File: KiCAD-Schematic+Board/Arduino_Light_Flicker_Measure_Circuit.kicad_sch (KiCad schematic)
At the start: 42 parts, among them J1 Ds, J2 Ds, J3 FTDI, J4 FTDI-Conn, J5 PWR(5V), J6 USB Power (5V), Q1 BC547, Q2 BC547, U1 ATmega328P-PU, U2 AD5242, U3 AD823A, U4 Display

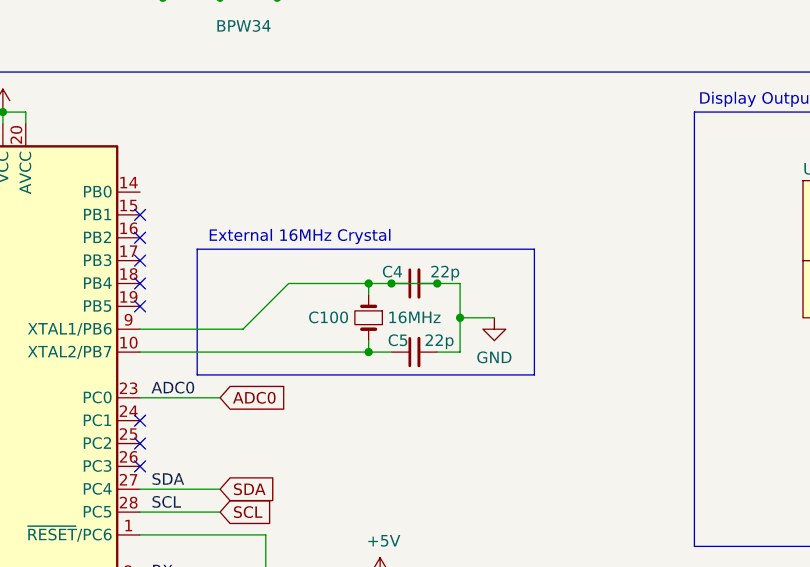
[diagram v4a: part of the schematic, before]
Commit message: Small update to add Pro Mini footprint to get rid of original footprint stuff hopefully.
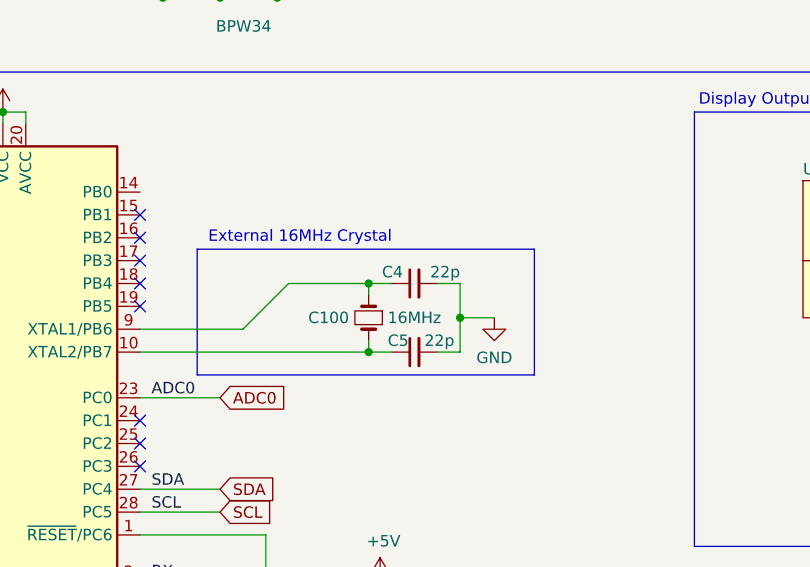
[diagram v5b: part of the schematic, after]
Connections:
- net GND: no longer C100.1, C4.1, U1.9 (XTAL1/PB6)
- new net: C100.1, C4.1, U1.9 (XTAL1/PB6)
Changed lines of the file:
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@@
   (junction (at 67.31 96.52) (diameter 0) (color 0 0 0 0)
   )
-  (junction (at 97.79 128.27) (diameter 0) (color 0 0 0 0)
-  )
   (junction (at 124.46 78.74) (diameter 0) (color 0 0 0 0)
   )
@@
   )
   (junction (at 49.53 109.22) (diameter 0) (color 0 0 0 0)
-  )
-  (junction (at 92.71 128.27) (diameter 0) (color 0 0 0 0)
   )
   (junction (at 80.01 82.55) (diameter 0) (color 0 0 0 0)
@@
     (stroke (width 0) (type default))
   )
+  (wire (pts (xy 97.79 128.27) (xy 100.33 128.27))
+    (stroke (width 0) (type default))
+  )
   (wire (pts (xy 82.55 46.99) (xy 82.55 63.5))
     (stroke (width 0) (type default))
@@
     (stroke (width 0) (type default))
   )
-  (wire (pts (xy 97.79 128.27) (xy 100.33 128.27))
-    (stroke (width 0) (type default))
-  )
   (wire (pts (xy 50.8 34.29) (xy 50.8 27.94))
     (stroke (width 0) (type default))
@@
     (stroke (width 0) (type default))
   )
-  (wire (pts (xy 92.71 128.27) (xy 90.17 128.27))
-    (stroke (width 0) (type default))
-  )
   (wire (pts (xy 158.75 97.79) (xy 158.75 91.44))
     (stroke (width 0) (type default))
@@
     (stroke (width 0) (type default))
   )
-  (wire (pts (xy 92.71 128.27) (xy 97.79 128.27))
-    (stroke (width 0) (type default))
-  )
   (wire (pts (xy 158.75 83.82) (xy 158.75 78.74))
     (stroke (width 0) (type default))
@@
     (stroke (width 0) (type default))
   )
+  (wire (pts (xy 90.17 128.27) (xy 92.71 128.27))
+    (stroke (width 0) (type default))
+  )

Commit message: Update to do basic messed-up layout.  Imperfect but hopefully functional.
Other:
- note added: "Digipot (0 or 1M) to ON/OFF 3 BPW34"
- note removed: "Digital Poti (0 or 1M) to ON/OFF 3 BPW34"
- moved on the sheet: J1
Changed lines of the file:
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@@
     (stroke (width 0) (type default))
   )
-  (wire (pts (xy 77.47 62.23) (xy 77.47 66.04))
+  (wire (pts (xy 77.47 62.23) (xy 77.47 64.77))
     (stroke (width 0) (type default))
   )
@@
     (stroke (width 0) (type default))
   )
-  (wire (pts (xy 82.55 66.04) (xy 82.55 63.5))
+  (wire (pts (xy 82.55 64.77) (xy 82.55 63.5))
     (stroke (width 0) (type default))
   )
@@
     (stroke (width 0) (type default))
   )
-  (wire (pts (xy 80.01 49.53) (xy 80.01 66.04))
+  (wire (pts (xy 80.01 49.53) (xy 80.01 64.77))
     (stroke (width 0) (type default))
   )
@@
     (effects (font (size 1.27 1.27)))
   )
-  (text "Digital Poti (0 or 1M)\nto ON/OFF 3 BPW34\n" (exclude_from_sim no)
+  (text "Digipot (0 or 1M)\nto ON/OFF 3 BPW34\n" (exclude_from_sim no)
  (at 88.9 43.815 0)
     (effects (font (size 1.27 1.27)))
@@
     )
   )
-  (symbol (lib_id "Connector_Generic:Conn_01x03") (at 80.01 71.12 90) (mirror x) (unit 1)
-    (exclude_from_sim no) (in_bom yes) (on_board yes) (dnp no)
-    (property "Reference" "J1" (at 84.7852 67.8942 90)
+  (symbol (lib_id "Connector_Generic:Conn_01x03") (at 80.01 69.85 90) (mirror x) (unit 1)
+    (exclude_from_sim no) (in_bom yes) (on_board yes) (dnp no)
+    (property "Reference" "J1" (at 84.7852 66.6242 90)
       (effects (font (size 1.27 1.27)) (justify right))
     )
-    (property "Value" "Ds" (at 84.7852 70.2056 90)
+    (property "Value" "Ds" (at 84.7852 68.9356 90)
       (effects (font (size 1.27 1.27)) (justify right))
     )
-    (property "Footprint" "Connector_PinHeader_2.54mm:PinHeader_1x03_P2.54mm_Vertical" (at 80.01 71.12 0)
-      (effects (font (size 1.27 1.27)) hide)
-    )
-    (property "Datasheet" "~" (at 80.01 71.12 0)
-      (effects (font (size 1.27 1.27)) hide)
-    )
-    (property "Description" "" (at 80.01 71.12 0)
-      (effects (font (size 1.27 1.27)) hide)
-    )
+    (property "Footprint" "Connector_PinHeader_2.54mm:PinHeader_1x03_P2.54mm_Vertical" (at 80.01 69.85 0)
+      (effects (font (size 1.27 1.27)) hide)
+    )
+    (property "Datasheet" "~" (at 80.01 69.85 0)
+      (effects (font (size 1.27 1.27)) hide)
+    )
+    (property "Description" "" (at 80.01 69.85 0)
+      (effects (font (size 1.27 1.27)) hide)
+    )
